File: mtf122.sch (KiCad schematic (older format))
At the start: 129 parts, among them J1 CONN_CAP_IBM_F, SW1 1,8, SW10 A,8, SW100 6,2, SW101 7,2, SW102 7,1, SW103 8,2, SW104 9,1, SW105 A,1, SW106 A,2, SW107 B,2, SW108 C,2, SW109 D,2, SW11 B,8, SW110 D,3, SW111 E,3, SW112 E,2, SW113 F,3, SW114 G,3, SW115 G,2, SW116 1,1, SW117 2,1, SW118 3,1, SW119 4,1, SW12 C,8, SW120 6,1, SW121 8,1, SW122 C,1, SW123 D,1, SW124 E,1, SW125 F,1, SW126 F,2, SW127 G,1, SW13 1,7, SW14 2,7, SW15 3,7, SW16 4,7, SW17 5,7, SW18 6,7, SW19 7,7, SW2 2,8, SW20 8,7, SW21 9,7, SW22 A,7, SW23 B,7, SW24 C,7, SW25 1,5, SW26 1,6, SW27 2,6, SW28 3,6, SW29 4,6, SW3 3,8, SW30 5,6, SW31 5,5, SW32 6,6, SW33 7,6, SW34 8,5, SW35 8,6, SW36 9,6, SW37 9,5, SW38 A,6, SW39 B,6, SW4 4,8, SW40 C,6, SW41 D,7, SW42 D,8, SW43 E,7, SW44 E,8, SW45 F,7, SW46 F,8, SW47 G,7, SW48 G,8, SW49 1,4, SW5 5,8, SW50 2,4, SW51 2,5, SW52 3,5, SW53 4,5, SW54 5,4, SW55 6,5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

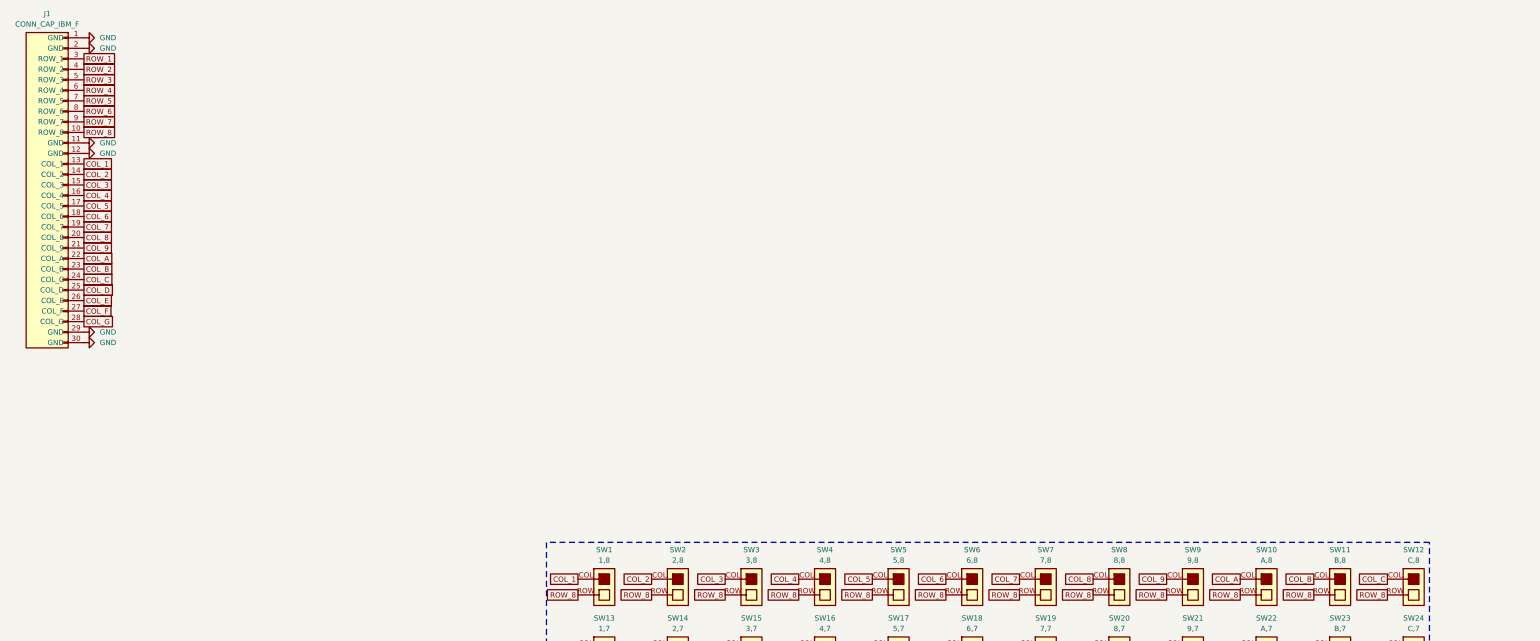
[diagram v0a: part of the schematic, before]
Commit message: Cleanup and schematic update
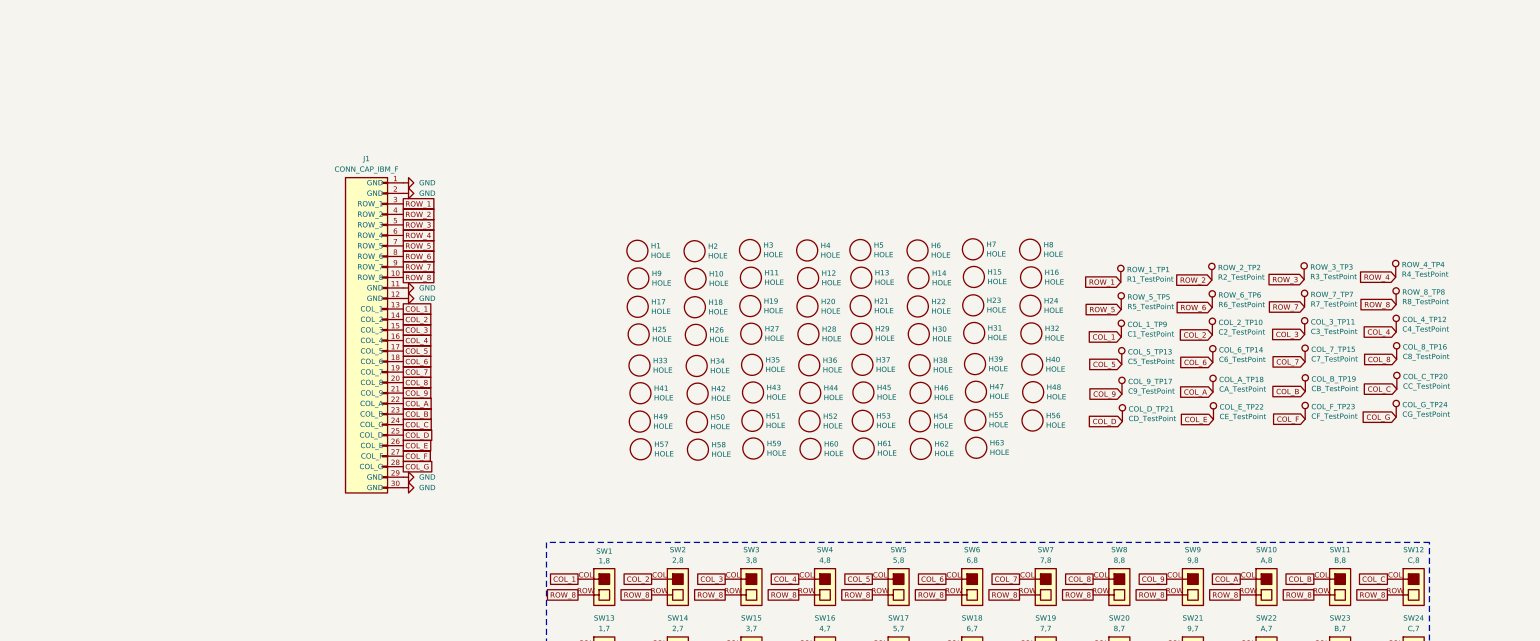
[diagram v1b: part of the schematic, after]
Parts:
- added COL_1_TP9: C1_TestPoint, TestPoint:TestPoint_Pad_D1.0mm, symbol Connector:TestPoint
- added COL_2_TP10: C2_TestPoint, TestPoint:TestPoint_Pad_D1.0mm, symbol Connector:TestPoint
- added COL_3_TP11: C3_TestPoint, TestPoint:TestPoint_Pad_D1.0mm, symbol Connector:TestPoint
- added COL_4_TP12: C4_TestPoint, TestPoint:TestPoint_Pad_D1.0mm, symbol Connector:TestPoint
- added COL_5_TP13: C5_TestPoint, TestPoint:TestPoint_Pad_D1.0mm, symbol Connector:TestPoint
- added COL_6_TP14: C6_TestPoint, TestPoint:TestPoint_Pad_D1.0mm, symbol Connector:TestPoint
- added COL_7_TP15: C7_TestPoint, TestPoint:TestPoint_Pad_D1.0mm, symbol Connector:TestPoint
- added COL_8_TP16: C8_TestPoint, TestPoint:TestPoint_Pad_D1.0mm, symbol Connector:TestPoint
- added COL_9_TP17: C9_TestPoint, TestPoint:TestPoint_Pad_D1.0mm, symbol Connector:TestPoint
- added COL_A_TP18: CA_TestPoint, TestPoint:TestPoint_Pad_D1.0mm, symbol Connector:TestPoint
- added COL_B_TP19: CB_TestPoint, TestPoint:TestPoint_Pad_D1.0mm, symbol Connector:TestPoint
- added COL_C_TP20: CC_TestPoint, TestPoint:TestPoint_Pad_D1.0mm, symbol Connector:TestPoint
- added COL_D_TP21: CD_TestPoint, TestPoint:TestPoint_Pad_D1.0mm, symbol Connector:TestPoint
- added COL_E_TP22: CE_TestPoint, TestPoint:TestPoint_Pad_D1.0mm, symbol Connector:TestPoint
- added COL_F_TP23: CF_TestPoint, TestPoint:TestPoint_Pad_D1.0mm, symbol Connector:TestPoint
- added COL_G_TP24: CG_TestPoint, TestPoint:TestPoint_Pad_D1.0mm, symbol Connector:TestPoint
- added H1, H10, H11, H12, H13, H14, H15, H16, H17, H18, H19, H2, H20, H21, H22, H23, H24, H25, H26, H27, H28, H29, H3, H30, H31, H32, H33, H34, H35, H36, H37, H38, H39, H4, H40, H41, H42, H43, H44, H45, H46, H47, H48, H49, H5, H50, H51, H52, H53, H54, H55, H56, H57, H58, H59, H6, H60, H61, H62, H63, H7, H8, H9: HOLE, lib_fp:HOLE, symbol lib_sch:HOLE
- added ROW_1_TP1: R1_TestPoint, TestPoint:TestPoint_Pad_D1.0mm, symbol Connector:TestPoint
- added ROW_2_TP2: R2_TestPoint, TestPoint:TestPoint_Pad_D1.0mm, symbol Connector:TestPoint
- added ROW_3_TP3: R3_TestPoint, TestPoint:TestPoint_Pad_D1.0mm, symbol Connector:TestPoint
- added ROW_4_TP4: R4_TestPoint, TestPoint:TestPoint_Pad_D1.0mm, symbol Connector:TestPoint
- added ROW_5_TP5: R5_TestPoint, TestPoint:TestPoint_Pad_D1.0mm, symbol Connector:TestPoint
- added ROW_6_TP6: R6_TestPoint, TestPoint:TestPoint_Pad_D1.0mm, symbol Connector:TestPoint
- added ROW_7_TP7: R7_TestPoint, TestPoint:TestPoint_Pad_D1.0mm, symbol Connector:TestPoint
- added ROW_8_TP8: R8_TestPoint, TestPoint:TestPoint_Pad_D1.0mm, symbol Connector:TestPoint
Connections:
- net COL_1: now also COL_1_TP9.1
- net COL_2: now also COL_2_TP10.1
- net COL_3: now also COL_3_TP11.1
- net COL_4: now also COL_4_TP12.1
- net COL_5: now also COL_5_TP13.1
- net COL_6: now also COL_6_TP14.1
- net COL_7: now also COL_7_TP15.1
- net COL_8: now also COL_8_TP16.1
- net COL_9: now also COL_9_TP17.1
- net COL_A: now also COL_A_TP18.1
- net COL_B: now also COL_B_TP19.1
- net COL_C: now also COL_C_TP20.1
- net COL_D: now also COL_D_TP21.1
- net COL_E: now also COL_E_TP22.1
- net COL_F: now also COL_F_TP23.1
- net COL_G: now also COL_G_TP24.1
- net ROW_1: now also ROW_1_TP1.1
- net ROW_2: now also ROW_2_TP2.1
- net ROW_3: now also ROW_3_TP3.1
- net ROW_4: now also ROW_4_TP4.1
- net ROW_5: now also ROW_5_TP5.1
- net ROW_6: now also ROW_6_TP6.1
- net ROW_7: now also ROW_7_TP7.1
- net ROW_8: now also ROW_8_TP8.1
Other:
- moved on the sheet: J1
